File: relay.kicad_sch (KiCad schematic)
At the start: 0 parts

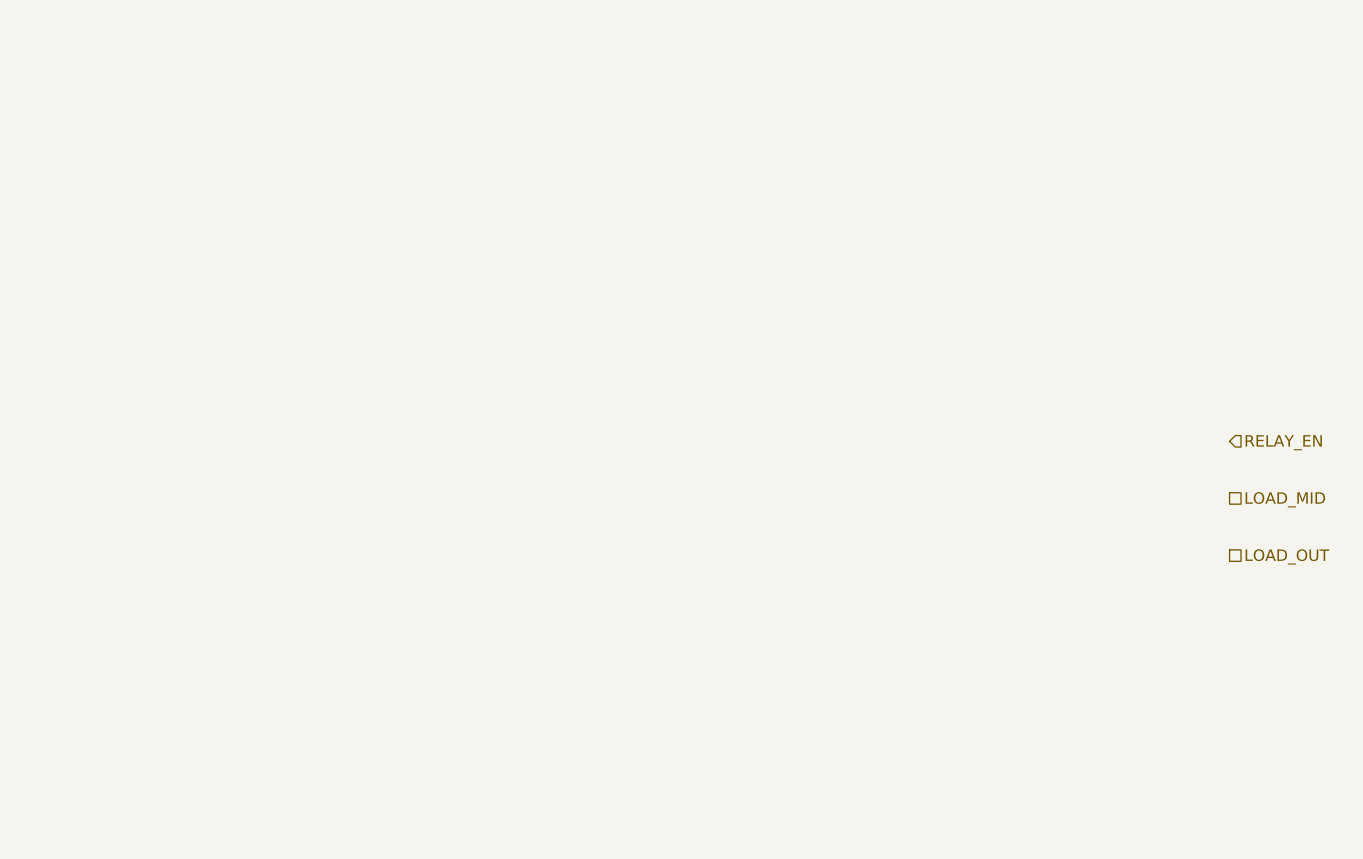
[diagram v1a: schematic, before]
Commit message: Add relay sheet
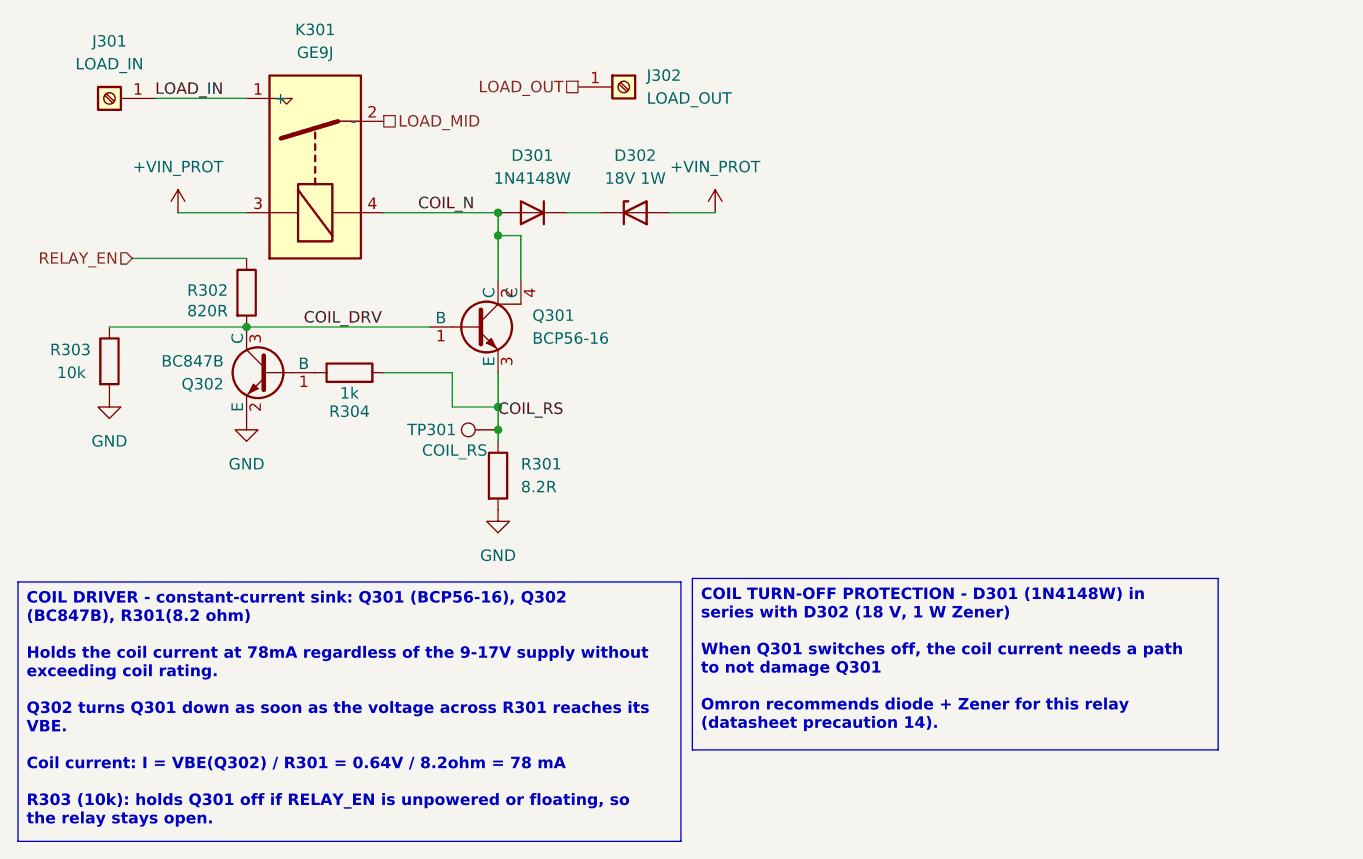
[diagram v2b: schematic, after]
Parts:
- added D301: 1N4148W, Diode_SMD:D_SOD-123, symbol Diode:1N4148W
- added D302: 18V 1W, Diode_SMD:D_SMA, symbol Device:D_Zener
- added J301: LOAD_IN, symbol Connector:Screw_Terminal_01x01
- added J302: LOAD_OUT, symbol Connector:Screw_Terminal_01x01
- added K301: GE9J, monitor:Relay_Omron_G9EJ-1-P-E, symbol monitor:GE9J-1-P-E-UVD
- added Q301: BCP56-16, Package_TO_SOT_SMD:SOT-223-3_TabPin2, symbol Transistor_BJT:BCP56
- added Q302: BC847B, Package_TO_SOT_SMD:SOT-23, symbol Transistor_BJT:BC847
- added R301: 8.2R, Resistor_SMD:R_0805_2012Metric, symbol Device:R
- added R302: 820R, Resistor_SMD:R_0603_1608Metric, symbol Device:R
- added R303: 10k, Resistor_SMD:R_0603_1608Metric, symbol Device:R
- added R304: 1k, Resistor_SMD:R_0603_1608Metric, symbol Device:R
- added TP301: COIL_RS, TestPoint:TestPoint_Pad_D1.5mm, symbol Connector:TestPoint
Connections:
- net LOAD_MID: now also K301.2 (-)
- net LOAD_OUT: now also J302.1 (Pin_1)
- net RELAY_EN: now also R302.1
- new net: D301.1 (K), D302.1 (K)
- new net: Q302.1 (B), R304.1
- new net +VIN_PROT: D302.2 (A), K301.3
- new net COIL_DRV: Q301.1 (B), Q302.3 (C), R302.2, R303.1
- new net COIL_N: D301.2 (A), K301.4, Q301.2 (C), Q301.4 (C)
- new net COIL_RS: Q301.3 (E), R301.1, R304.2, TP301.1
- new net GND: Q302.2 (E), R301.2, R303.2
- new net LOAD_IN: J301.1 (Pin_1), K301.1 (+)

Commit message: Fix relay symbol link, add load terminals and mounting holes
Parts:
- J301, J302: footprint (none) -> MountingHole:MountingHole_4.3mm_M4_Pad
- K301: value GE9J -> G9EJ-1-P-E-UVD DC12
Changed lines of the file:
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@@
 			)
 		)
-		(property "Value" "GE9J"
+		(property "Value" "G9EJ-1-P-E-UVD DC12"
 			(at 48.26 24.13 90)
 			(show_name no)
@@
 			)
 		)
-		(property "Footprint" ""
+		(property "Footprint" "MountingHole:MountingHole_4.3mm_M4_Pad"
 			(at 25.4 29.21 0)
 			(hide yes)
@@
 			)
 		)
-		(property "Footprint" ""
+		(property "Footprint" "MountingHole:MountingHole_4.3mm_M4_Pad"
 			(at 82.55 27.94 0)
 			(hide yes)

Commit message: Fix relay value and Q301 footprint
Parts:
- K301: symbol monitor:GE9J-1-P-E-UVD -> monitor:G9EJ
- Q301: footprint Package_TO_SOT_SMD:SOT-223-3_TabPin2 -> Package_TO_SOT_SMD:SOT-223
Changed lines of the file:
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@@
 			)
 		)
-		(property "Footprint" "Package_TO_SOT_SMD:SOT-223-3_TabPin2"
+		(property "Footprint" "Package_TO_SOT_SMD:SOT-223"
 			(at 71.12 56.515 0)
 			(hide yes)
@@
 	)
 	(symbol
-		(lib_id "monitor:GE9J-1-P-E-UVD")
+		(lib_id "monitor:G9EJ")
 		(at 48.26 36.83 90)
 		(unit 1)
